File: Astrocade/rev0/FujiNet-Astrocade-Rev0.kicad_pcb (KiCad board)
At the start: 6 copper layers, 96 x 58 mm, 87 parts, among them J1 Astrocade_Cart_Edge_26, J2 microSD, J3 USB-C, SW1 RESET, SW2 BOOTSEL, SW3 S3_RST, SW4 S3_BOOT, U1 RP2354A, U2 ESP32-S3-WROOM-1-N16R8, U3 CP2102N-A02-GQFN28, U4 UMH3N, U5 AP63203WU, Y1 12MHz

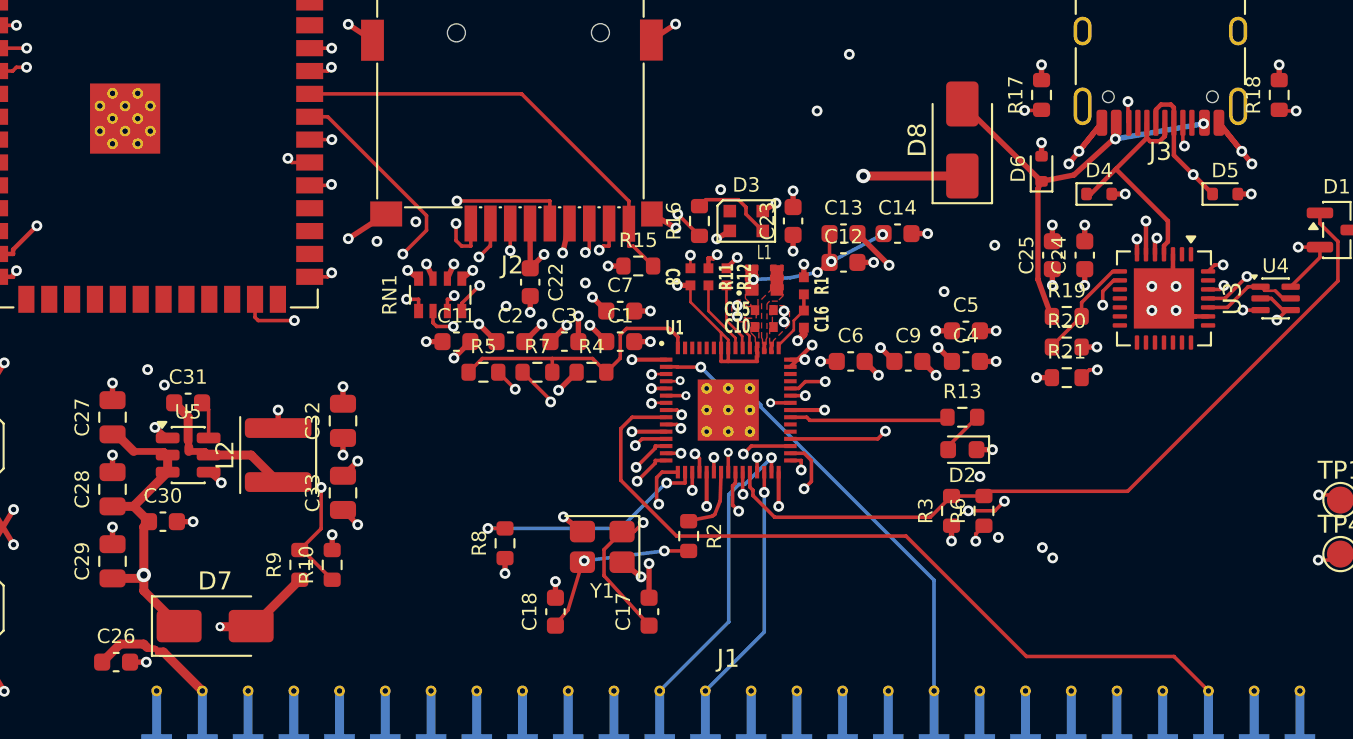
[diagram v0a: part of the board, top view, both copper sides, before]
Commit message: Astrocade Rev0: merge RP2350 corner GND into top pour; tidy tracks
Review feedback on PR 45:
- The small GND pour grafted from Raspberry Pi's layout NE of the RP2354A
  read as an isolated ground island (it was via-tied, but separate). It is
  dropped; the board-wide top GND pour now fills that corner, solidly
  connected to C10/C15/C16 and U1's PGND/EP (DRU rp2350_core_gnd_solid,
  pour clearance 0.15 mm). A 0.1 mm^2 top-pour sliver there is gone and the
  RP's exposed-pad area joins the main pour.
- New tools/tidy_tracks.py (also in build_all.sh) removes router artifacts
  around the RP without rerouting: tiny/in-pad stubs, 3 fold-back
  segments, collinear splits, and an acute DVDD corner. Every step is
  DRC-checked and reverted if it adds an error.

DRC 0 errors / 0 unconnected / 0 parity, ERC 0, check_nets 174/174.
Fab outputs and renders re-exported.

Co-Authored-By: Claude Opus 5.5 (1M context) <noreply@anthropic.com>
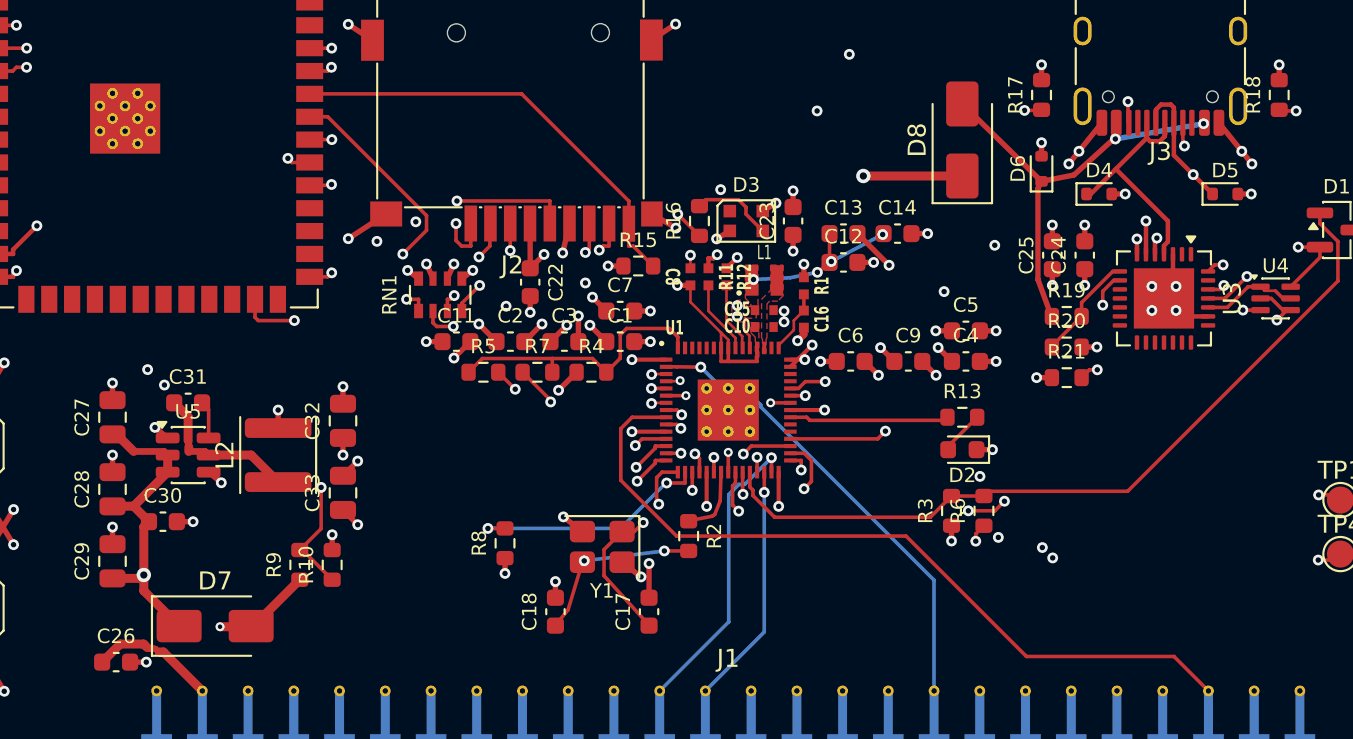
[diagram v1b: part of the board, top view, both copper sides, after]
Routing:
- net GND: track 87.3 -> 83.2 mm

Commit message: Astrocade Rev0: audit with kicad-happy + datasheets and redo
Schematic, board and fab outputs regenerated from tools/ after a
datasheet-level audit (docs/design-review-rev0.md).

Design fixes:
- RP2354A on its own AP2112K rail (+3V3_RP): its FT pads take 5.5 V only
  with IOVDD powered (RP2350 DS p.1332); the buck's UVLO + 4 ms soft-start
  left them unpowered while the console drove the bus
- WS2812B-2020-V6 on +5V (datasheet VDD 3.7-5.3 V, not a 3.3 V part)
- VBUS decoupling at the USB-C, activity LED 330R, card-detect polarity
  settled (low = card present), fiducials, RUN/BOOTSEL/rail test pads

Schematic redrawn readably: root block diagram with hierarchical pins,
power symbols, wired clusters and design notes (tools/sch_layout.py);
check_sch_layout.py proves the drawn netlist equals design.py.

Board: 4 layers tried first and did not close; 6 layers, 100% routed,
DRC 0 errors / 0 unconnected / 0 parity. Locked USB-C D+/D- pad ties,
GND stitching kept out of pads, return vias at USB/crystal layer
changes, check_vias.py gate (KiCad re-nets a via inside another net's
pad, so its DRC cannot see it).

Co-Authored-By: Claude Opus 5.5 <noreply@anthropic.com>
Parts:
- added C34: 22uF, FujiNet-Astrocade:C_0805_2012Metric, F.Cu at (78.6, 55.6)
- added C35: 22uF, FujiNet-Astrocade:C_0805_2012Metric, F.Cu at (78.6, 59.6)
- added C36: 1uF, FujiNet-Astrocade:C_0603_1608Metric, F.Cu at (81.0, 66.5)
- added C37: 1uF, FujiNet-Astrocade:C_0603_1608Metric, F.Cu at (88.0, 66.5)
- added FID1: Fiducial_1mm_Mask2mm, FujiNet-Astrocade:Fiducial_1mm_Mask2mm, F.Cu at (139.0, 32.2)
- added FID2: Fiducial_1mm_Mask2mm, FujiNet-Astrocade:Fiducial_1mm_Mask2mm, F.Cu at (60.5, 75.0)
- added FID3: Fiducial_1mm_Mask2mm, FujiNet-Astrocade:Fiducial_1mm_Mask2mm, F.Cu at (139.5, 75.0)
- added TP10: +3V3_RP, FujiNet-Astrocade:TestPoint_Pad_D1.5mm, F.Cu at (120.6, 67.6)
- added TP6: RUN, FujiNet-Astrocade:TestPoint_Pad_D1.5mm, F.Cu at (139.6, 63.0)
- added TP7: BOOTSEL, FujiNet-Astrocade:TestPoint_Pad_D1.5mm, F.Cu at (142.4, 63.0)
- added TP8: +5V, FujiNet-Astrocade:TestPoint_Pad_D1.5mm, F.Cu at (62.0, 67.0)
- added TP9: +3V3, FujiNet-Astrocade:TestPoint_Pad_D1.5mm, F.Cu at (142.4, 60.0)
- added U6: AP2112K-3.3, FujiNet-Astrocade:SOT-23-5, F.Cu at (84.5, 66.5)
- C24: value 100nF -> 1uF
- C25: value 4.7uF -> 100nF
- C27: value 22uF -> 4.7uF; footprint FujiNet-Astrocade:C_0805_2012Metric -> FujiNet-Astrocade:C_0603_1608Metric
- C28, C32, C33: value 22uF -> 100nF; footprint FujiNet-Astrocade:C_0805_2012Metric -> FujiNet-Astrocade:C_0603_1608Metric
- C30, C31: value 100nF -> 22uF; footprint FujiNet-Astrocade:C_0603_1608Metric -> FujiNet-Astrocade:C_0805_2012Metric
- D1: value BAT54C -> green; footprint FujiNet-Astrocade:SOT-23 -> FujiNet-Astrocade:LED_0603_1608Metric
- D2: value green -> BAT54C; footprint FujiNet-Astrocade:LED_0603_1608Metric -> FujiNet-Astrocade:SOT-23
- R13: value 1k -> 330R
- SW1: value RESET -> BOOTSEL
- SW2: value BOOTSEL -> S3_RST
- SW3: value S3_RST -> S3_BOOT
- SW4: value S3_BOOT -> RESET
- moved SW4 87.1 mm to (141.0, 43.0), turned to 0 degrees
- moved SW2 84.1 mm to (57.0, 57.0), turned to 90 degrees
- moved C26 58.4 mm to (119.8, 46.4), turned to 90 degrees
- moved C27 53.0 mm to (118.0, 46.4)
- moved D1 24.1 mm to (113.0, 57.2), turned to 180 degrees
- moved D2 24.1 mm to (133.8, 45.0), turned to 0 degrees
- moved C24 12.6 mm to (109.6, 39.0), turned to 0 degrees
- moved C32 11.5 mm to (68.6, 61.2), turned to 0 degrees
- moved C25 9.99 mm to (109.6, 41.0), turned to 0 degrees
- moved C33 9.95 mm to (70.0, 54.6), turned to 0 degrees
- moved C31 9.75 mm to (65.8, 63.4), turned to 90 degrees
- moved C28 9.60 mm to (66.0, 69.0), turned to 0 degrees
- moved SW1 9.00 mm to (141.0, 52.0)
- moved SW3 9.00 mm to (57.0, 66.0)
- moved C29 8.00 mm to (65.8, 55.4)
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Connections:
- net BOOTSEL_CTL renamed /cart/BOOTSEL_CTL
- net CA0 renamed /cart/CA0
- net CA1 renamed /cart/CA1
- net CA10 renamed /cart/CA10
- net CA11 renamed /cart/CA11
- net CA12 renamed /cart/CA12
- net CA2 renamed /cart/CA2
- net CA3 renamed /cart/CA3
- net CA4 renamed /cart/CA4
- net CA5 renamed /cart/CA5
- net CA6 renamed /cart/CA6
- net CA7 renamed /cart/CA7
- net CA8 renamed /cart/CA8
- net CA9 renamed /cart/CA9
- net CC1 renamed /usb/CC1
- net CC2 renamed /usb/CC2
- net CCS_N renamed /cart/CCS_N
- net CD0 renamed /cart/CD0
- net CD1 renamed /cart/CD1
- net CD2 renamed /cart/CD2
- net CD3 renamed /cart/CD3
- net CD4 renamed /cart/CD4
- net CD5 renamed /cart/CD5
- net CD6 renamed /cart/CD6
- net CD7 renamed /cart/CD7
- net CP_RST renamed /usb/CP_RST
- net LED_STRIP renamed /esp32/LED_STRIP
- net QSPI_SS renamed /cart/QSPI_SS
- net RP_DBG_TX renamed /cart/RP_DBG_TX
- net RP_LED renamed /cart/RP_LED
- net RP_LX renamed /cart/RP_LX
- net RP_USB_DM renamed /cart/RP_USB_DM
- net RP_USB_DP renamed /cart/RP_USB_DP
- net RUN_CTL renamed /cart/RUN_CTL
- net S3_RXD renamed /esp32/S3_RXD
- net S3_TXD renamed /esp32/S3_TXD
- net SD_CD renamed /esp32/SD_CD
- net SD_CS renamed /esp32/SD_CS
- net SD_DAT1 renamed /esp32/SD_DAT1
- net SD_DAT2 renamed /esp32/SD_DAT2
- net SD_MISO renamed /esp32/SD_MISO
- net SD_MOSI renamed /esp32/SD_MOSI
- net SD_SCK renamed /esp32/SD_SCK
- net SELFTEST renamed /cart/SELFTEST
- net SWCLK renamed /cart/SWCLK
- net SWDIO renamed /cart/SWDIO
- net UART_DTR renamed /usb/UART_DTR
- net UART_RTS renamed /usb/UART_RTS
- net UBRG_DM renamed /usb/UBRG_DM
- net UBRG_DP renamed /usb/UBRG_DP
- net USB_DM renamed /cart/USB_DM
- net USB_DP renamed /cart/USB_DP
- net VBUS_SNS renamed /usb/VBUS_SNS
- net VREG_AVDD renamed /cart/VREG_AVDD
- net VSENSE renamed /cart/VSENSE
- net WS_DIN renamed /esp32/WS_DIN
- net XIN renamed /cart/XIN
- net XOUT renamed /cart/XOUT
- net XOUT_Y renamed /cart/XOUT_Y
- C1 pad 1: +3V3 -> +3V3_RP
- C10 pad 1: +3V3 -> +3V3_RP
- C11 pad 1: +3V3 -> +3V3_RP
- C2 pad 1: +3V3 -> +3V3_RP
- C21 pad 1: S3_EN -> /esp32/S3_EN
- C23 pad 1: +3V3 -> +5V
- C24 pad 1: +3V3 -> VBUS
- C25 pad 1: +3V3 -> VBUS
- C26 pad 1: +5V -> +3V3
- C27 pad 1: VIN -> +3V3
- C28 pad 1: VIN -> CONS_5V
- C29 pad 1: VIN -> +5V
- C3 pad 1: +3V3 -> +3V3_RP
- C30 pad 1: VIN -> +5V
- C31 pad 1: BUCK_SW -> +5V
- C31 pad 2: BUCK_BST -> GND
- C32 pad 1: +3V3 -> +5V
- C33 pad 1: +3V3 -> /power/BUCK_SW
- C33 pad 2: GND -> /power/BUCK_BST
- C4 pad 1: +3V3 -> +3V3_RP
- C5 pad 1: +3V3 -> +3V3_RP
- C6 pad 1: +3V3 -> +3V3_RP
- C7 pad 1: +3V3 -> +3V3_RP
- C8 pad 1: +3V3 -> +3V3_RP
- C9 pad 1: +3V3 -> +3V3_RP
- D1 pad 1: RUN -> GND
- D1 pad 2: S3_EN -> /cart/RP_LED_A
- D2 pad 1: GND -> /cart/RUN
- D2 pad 2: RP_LED_A -> /esp32/S3_EN
- D3 pad 4: +3V3 -> +5V
- D7 pad 1: VIN -> +5V
- D7 pad 2: +5V -> CONS_5V
- D8 pad 1: VIN -> +5V
- J1 pad 25: +5V -> CONS_5V
- L2 pad 1: BUCK_SW -> /power/BUCK_SW
- R1 pad 1: +3V3 -> +3V3_RP
- R13 pad 2: RP_LED_A -> /cart/RP_LED_A
- R14 pad 2: S3_EN -> /esp32/S3_EN
- R3 pad 1: +3V3 -> +3V3_RP
- R3 pad 2: RUN -> /cart/RUN
- R4 pad 1: +3V3 -> +3V3_RP
- R5 pad 2: BOOTSEL_BTN -> /cart/BOOTSEL_BTN
- R6 pad 2: RUN -> /cart/RUN
- R8 pad 1: +3V3 -> +3V3_RP
- R9 pad 1: +5V -> CONS_5V
- SW1 pad 1: RST_BTN -> /cart/BOOTSEL_BTN
- SW2 pad 1: BOOTSEL_BTN -> /esp32/S3_EN
- SW3 pad 1: S3_EN -> /esp32/S3_IO0
- SW4 pad 1: S3_IO0 -> /esp32/RST_BTN
- U1 pad 1: +3V3 -> +3V3_RP
- U1 pad 11: +3V3 -> +3V3_RP
- U1 pad 20: +3V3 -> +3V3_RP
- U1 pad 26: RUN -> /cart/RUN
- U1 pad 30: +3V3 -> +3V3_RP
- U1 pad 38: +3V3 -> +3V3_RP
- U1 pad 44: +3V3 -> +3V3_RP
- U1 pad 45: +3V3 -> +3V3_RP
- U1 pad 49: +3V3 -> +3V3_RP
- U1 pad 53: +3V3 -> +3V3_RP
- U1 pad 54: +3V3 -> +3V3_RP
- U2 pad 27: S3_IO0 -> /esp32/S3_IO0
- U2 pad 3: S3_EN -> /esp32/S3_EN
- U4 pad 3: S3_IO0 -> /esp32/S3_IO0
- U4 pad 6: S3_EN -> /esp32/S3_EN
- U5 pad 2: VIN -> +5V
- U5 pad 3: VIN -> +5V
- U5 pad 5: BUCK_SW -> /power/BUCK_SW
- U5 pad 6: BUCK_BST -> /power/BUCK_BST
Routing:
- net S3_EN: track 112.0 -> 0.00 mm, vias 3 -> 0
- net /esp32/S3_EN: track 0.00 -> 111.3 mm, vias 0 -> 3
- net /esp32/S3_IO0: track 0.00 -> 92.8 mm, vias 0 -> 3
- net S3_IO0: track 92.3 -> 0.00 mm, vias 3 -> 0
- net VIN: track 74.7 -> 0.00 mm, vias 2 -> 0
- net +5V: track 16.5 -> 90.3 mm, vias 1 -> 2
- net /cart/RUN: track 0.00 -> 63.3 mm, vias 0 -> 2
- net BOOTSEL_BTN: track 61.8 -> 0.00 mm, vias 2 -> 0
- net /cart/BOOTSEL_BTN: track 0.00 -> 61.1 mm, vias 0 -> 2
- net /cart/QSPI_SS: track 15.6 -> 67.1 mm, vias 0 -> 2
- net RUN: track 44.0 -> 0.00 mm
- net +3V3_RP: track 0.00 -> 39.0 mm, vias 0 -> 24
- net +3V3: track 59.2 -> 22.6 mm, vias 42 -> 20
- net CONS_5V: track 0.00 -> 16.9 mm, vias 0 -> 1
- net RST_BTN: track 12.1 -> 0.00 mm
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- added copper zone on F.Cu, net +3V3_RP
- added copper zone on In4.Cu, net +3V3_RP
- removed copper zone on F.Cu, net +3V3
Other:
- board text removed: "contacts: keep clean"

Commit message: Astrocade Rev0: redraw the schematic wired (5200 style), re-audit (#53)
The schematic was readable but disconnected: every edge land and RP GPIO
ended in a label and the RP's decoupling stood in a row away from its pins.
Port the FujiNet-5200 drawing pipeline (sch_draw / sch_draft / sch_place /
netlist) and hand-draw every sheet the way the later carts are drawn:

- root: the board outline at 2:1, each sheet's block over its region, the
  nine inter-sheet signals wired without a crossing
- cart-bus: the 26-land edge straight into the RP2354A's GPIO unit
  (22 parallel wires, no crossings); rp-core: every supply pin wired to
  its own capacitor and rail; fujinet, usb, power: all wired
- RP2354A split into two units; references frozen in tools/refs.lock,
  net names in tools/nets.lock

The routed board is unchanged: tools/sync_pcb_nets.py renames the board's
nets to the new sheet paths (self-checked), sync_pcb_sheets.py re-points
the footprint links. DRC with schematic parity 0/0/0, ERC 0, netlist
parity 74/74, check_nets 182/182; CPL byte-identical, gerbers identical
but for names and dates. build_all.sh now keeps the routed board by
default (LAYOUT=1 re-routes).

Re-audit (design review Part 3, deep review 25/25 gated, datasheets from
the sibling carts): VSENSE divider 100k/150k -> 10k/15k so RP2350-E9 (A2
silicon) cannot hold the serve gate open in a switched-off console (value
change only, same lands). DVDD decoupling, a VBUS pull-down, the activity
LED and the core inductor's stock are Rev1 / bring-up notes.

Co-authored-by: Claude Opus 5.5 <noreply@anthropic.com>
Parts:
- R10: value 150k -> 15k
- R9: value 100k -> 10k
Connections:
- net /cart/BOOTSEL_BTN renamed /rp-core/BOOTSEL_BTN
- net /cart/BOOTSEL_CTL renamed /BOOTSEL_CTL
- net /cart/CA0 renamed /cart-bus/CA0
- net /cart/CA1 renamed /cart-bus/CA1
- net /cart/CA10 renamed /cart-bus/CA10
- net /cart/CA11 renamed /cart-bus/CA11
- net /cart/CA12 renamed /cart-bus/CA12
- net /cart/CA2 renamed /cart-bus/CA2
- net /cart/CA3 renamed /cart-bus/CA3
- net /cart/CA4 renamed /cart-bus/CA4
- net /cart/CA5 renamed /cart-bus/CA5
- net /cart/CA6 renamed /cart-bus/CA6
- net /cart/CA7 renamed /cart-bus/CA7
- net /cart/CA8 renamed /cart-bus/CA8
- net /cart/CA9 renamed /cart-bus/CA9
- net /cart/CCS_N renamed /cart-bus/CCS_N
- net /cart/CD0 renamed /cart-bus/CD0
- net /cart/CD1 renamed /cart-bus/CD1
- net /cart/CD2 renamed /cart-bus/CD2
- net /cart/CD3 renamed /cart-bus/CD3
- net /cart/CD4 renamed /cart-bus/CD4
- net /cart/CD5 renamed /cart-bus/CD5
- net /cart/CD6 renamed /cart-bus/CD6
- net /cart/CD7 renamed /cart-bus/CD7
- net /cart/QSPI_SS renamed /rp-core/QSPI_SS
- net /cart/RP_DBG_TX renamed /cart-bus/RP_DBG_TX
- net /cart/RP_LED renamed /cart-bus/RP_LED
- net /cart/RP_LED_A renamed /cart-bus/RP_LED_A
- net /cart/RP_LX renamed /rp-core/RP_LX
- net /cart/RP_USB_DM renamed /rp-core/RP_USB_DM
- net /cart/RP_USB_DP renamed /rp-core/RP_USB_DP
- net /cart/RUN renamed /rp-core/RUN
- net /cart/RUN_CTL renamed /RUN_CTL
- net /cart/SELFTEST renamed /cart-bus/SELFTEST
- net /cart/SWCLK renamed /rp-core/SWCLK
- net /cart/SWDIO renamed /rp-core/SWDIO
- net /cart/USB_DM renamed /USB_DM
- net /cart/USB_DP renamed /USB_DP
- net /cart/VREG_AVDD renamed /rp-core/VREG_AVDD
- net /cart/VSENSE renamed /cart-bus/VSENSE
- net /cart/XIN renamed /rp-core/XIN
- net /cart/XOUT renamed /rp-core/XOUT
- net /cart/XOUT_Y renamed /rp-core/XOUT_Y
- net /esp32/LED_STRIP renamed /fujinet/LED_STRIP
- net /esp32/RST_BTN renamed /rp-core/RST_BTN
- net /esp32/S3_EN renamed /S3_EN
- net /esp32/S3_IO0 renamed /S3_IO0
- net /esp32/S3_RXD renamed /S3_RXD
- net /esp32/S3_TXD renamed /S3_TXD
- net /esp32/SD_CD renamed /fujinet/SD_CD
- net /esp32/SD_CS renamed /fujinet/SD_CS
- net /esp32/SD_DAT1 renamed /fujinet/SD_DAT1
- net /esp32/SD_DAT2 renamed /fujinet/SD_DAT2
- net /esp32/SD_MISO renamed /fujinet/SD_MISO
- net /esp32/SD_MOSI renamed /fujinet/SD_MOSI
- net /esp32/SD_SCK renamed /fujinet/SD_SCK
- net /esp32/WS_DIN renamed /fujinet/WS_DIN

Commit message: Astrocade Rev0: re-plot the fab zip from refilled zones, drop 3 stray vias
The JLCPCB zip put 161 plated holes inside an inner pour of another net: GND vias inside the In4 +3V3 pours, and USB_DP and CD7 inside the In1 GND through two GND stitching vias that sat on their tracks (a third on a +3V3 track; KiCad re-nets such a via to the track on load, so DRC never saw them). The three vias are removed (382 -> 379, the via_dangling warning gone, still 0 unconnected), and check_vias.py now tests tracks as well as pads. Now 0.

The gerbers are plotted from the zone fills saved in the board file, and
stitch_gnd.py adds its GND vias after the last fill, so the saved inner
pours still covered them; the DRC gate (--refill-zones, fresh fills in
memory) passed. Found on FujiNet-StudioII Rev0.

- the board refilled and saved (tools/fill_zones.py); outside the zone
  fills it is unchanged (parsed, attribute order ignored); KiCad DRC on the
  saved fills gives the same result as the old gate
- pipeline: fill_zones before the DRC gate, the gate on the saved fills,
  export with --check-zones, tools/audit/check_plane_shorts.py on the zips
- re-exported: only the copper layers changed; renders and layout SVGs
  follow the refilled pours; PDFs whose only change was KiCad's version
  stamp reverted

Co-Authored-By: Claude Opus 5.5 <noreply@anthropic.com>
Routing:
- net GND: vias 237 -> 234
